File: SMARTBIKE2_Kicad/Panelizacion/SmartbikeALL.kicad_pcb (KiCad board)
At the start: 2 copper layers, 100 x 100 mm, 101 parts, among them IC1 ESP32-WROVER-B__8MB_, J1 Conn_01x02, J1 Conn_01x08, J2 Conn_01x01, J2 Conn_01x02, J2 RJ45, J3 Conn_02x03_Counter_Clockwise, J4 Conn_01x04, J5 Conn_01x05, J6 Conn_01x08, J7 Conn_01x08, J8 Conn_01x04, Q1 SI2302, Q2 FDN340P, Q3 SI2302, Q4 SI2302, Q5 SI2302, SW1 SW_Boot, SW2 SW_Reset, U1 MIC5219-3.3YM5, U1 NA555D, U2 LM358, U2 MIC29302WU, U3 MIC5219-3.3YM5, U4 NA555D

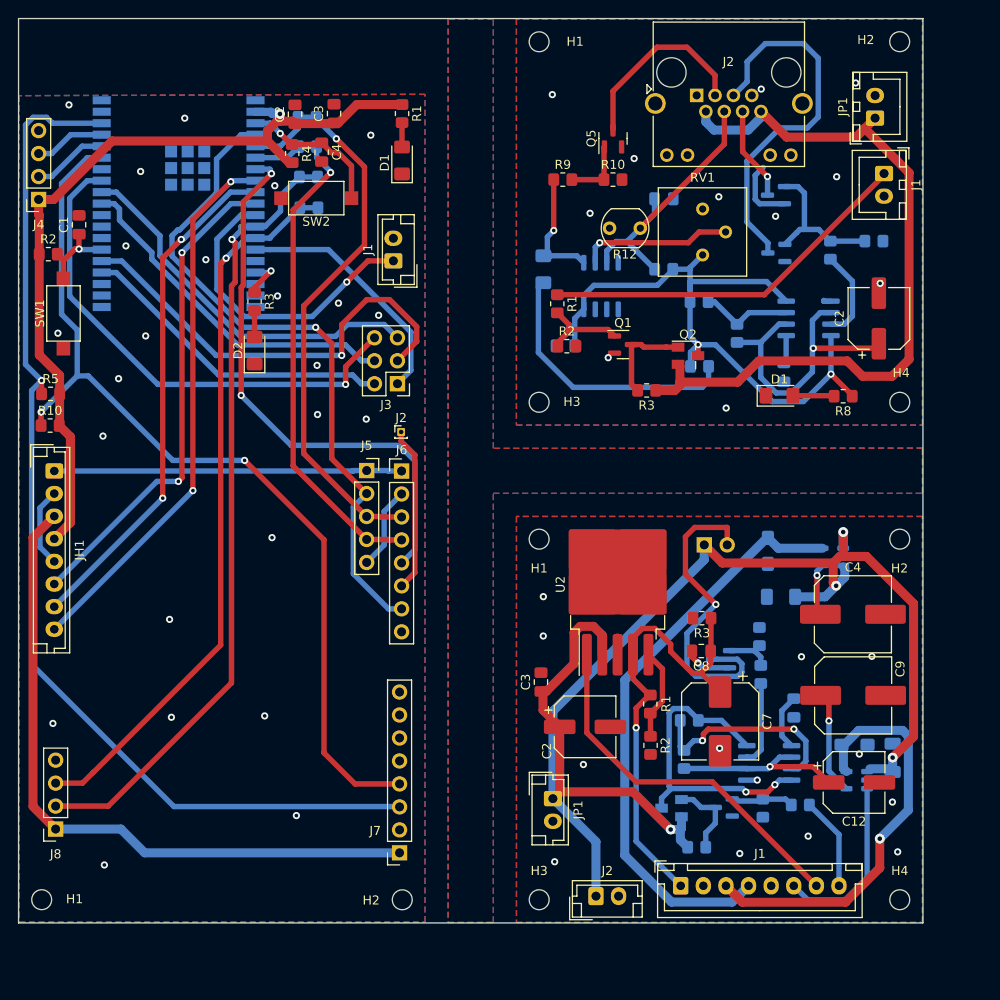
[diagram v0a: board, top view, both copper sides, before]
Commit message: Impresión vías sin metalización
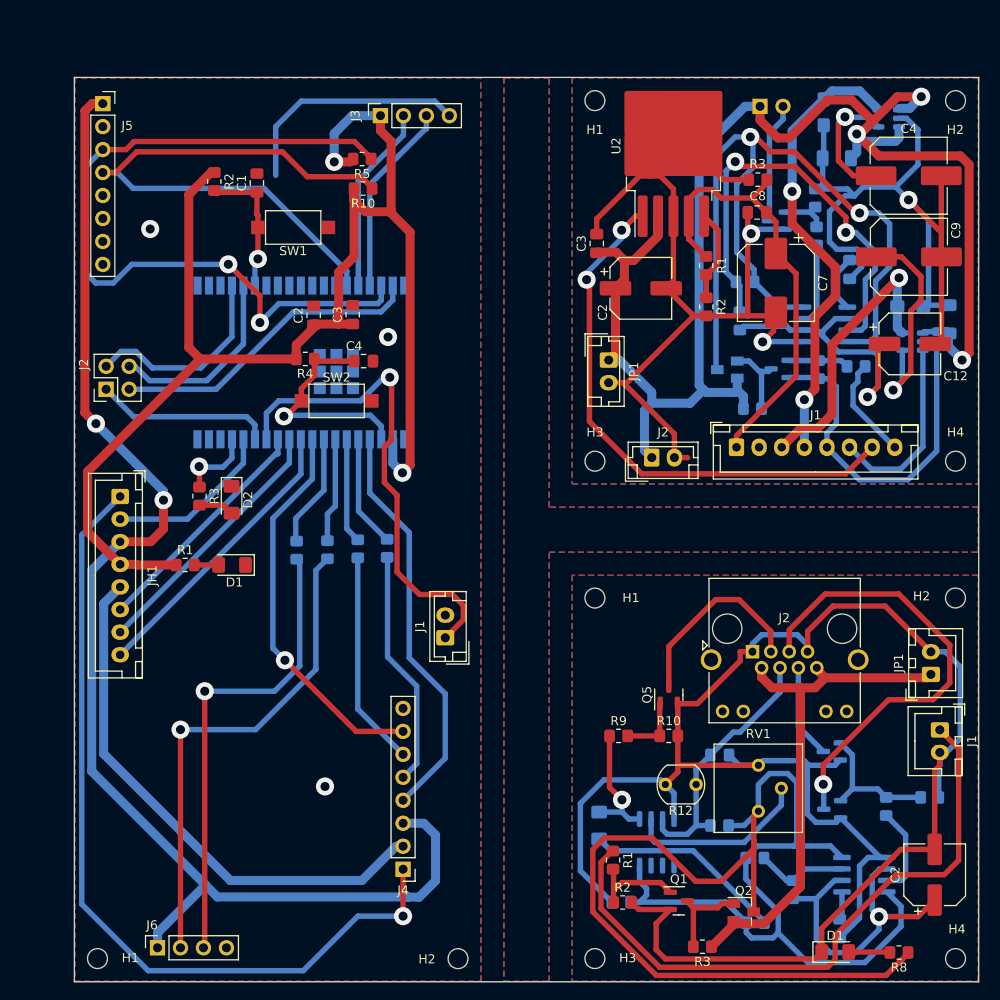
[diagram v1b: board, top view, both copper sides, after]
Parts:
- removed the C1 at (115.7, 40.8)
- removed the C1 at (193.6, 57.1)
- removed the C1 at (193.3, 81.9)
- removed the C2 at (171.6, 96.3)
- removed the C2 at (139.5, 28.5)
- removed the C2 at (204.1, 51.1)
- removed the C3 at (143.9, 28.5)
- removed the C3 at (166.7, 91.3)
- removed the C3 at (169.4, 54.1)
- removed the C4 at (201.2, 83.8)
- removed the C4 at (142.5, 32.7)
- removed the C4 at (180.3, 37.9)
- removed the D1 at (193.1, 59.7)
- removed the D1 at (151.4, 33.6)
- removed the D2 at (135.1, 54.7)
- removed the D2 at (167.0, 45.7)
- removed the H1 at (166.5, 75.5)
- removed the H1 at (166.5, 20.5)
- removed the H1 at (111.5, 115.4)
- removed the H2 at (206.4, 75.5)
- removed the H2 at (206.4, 20.5)
- removed the H2 at (151.4, 115.4)
- removed the H3 at (166.5, 60.4)
- removed the H3 at (166.5, 115.4)
- removed the H4 at (206.4, 60.4)
- removed the H4 at (206.4, 115.4)
- removed the J1 at (150.4, 44.7)
- removed the J1 at (204.7, 35.1)
- removed the J1 at (182.2, 113.8)
- removed the J2 at (151.3, 63.7)
- removed the J2 at (184.0, 26.4)
- removed the J2 at (172.8, 115.0)
- removed J7: Conn_01x08, Connector_PinSocket_2.54mm:PinSocket_1x08_P2.54mm_Vertical
- removed J8: Conn_01x04, Connector_PinSocket_2.54mm:PinSocket_1x04_P2.54mm_Vertical
- removed the JP1 at (168.1, 104.2)
- removed the JP1 at (203.7, 29.0)
- removed the Q1 at (175.8, 54.0)
- removed the Q1 at (187.0, 105.2)
- removed the Q2 at (183.0, 55.2)
- removed the Q2 at (181.2, 105.3)
- removed the Q3 at (192.7, 37.5)
- removed the Q3 at (186.7, 88.8)
- removed the R1 at (178.8, 93.8)
- removed the R1 at (151.4, 28.5)
- removed the R1 at (168.5, 49.5)
- removed the R10 at (112.5, 63.0)
- removed the R10 at (174.7, 35.8)
- removed the R10 at (190.9, 86.3)
- removed the R2 at (169.6, 54.2)
- removed the R2 at (178.8, 98.3)
- removed the R2 at (112.3, 44.0)
- removed the R3 at (184.5, 84.3)
- removed the R3 at (135.1, 49.2)
- removed the R3 at (178.4, 59.1)
- removed the R4 at (139.2, 32.9)
- removed the R4 at (198.7, 43.6)
- removed the R4 at (195.4, 104.9)
- removed the R5 at (112.5, 59.4)
- removed the R5 at (191.3, 105.3)
- removed the R5 at (203.6, 42.6)
- removed the R6 at (184.2, 49.3)
- removed the R6 at (184.0, 109.6)
- removed the R6 at (140.9, 28.9)
- removed the R7 at (140.9, 32.1)
- removed the R7 at (188.4, 52.8)
- removed the R7 at (183.1, 95.6)
- removed the R8 at (200.2, 59.7)
- removed the R8 at (141.0, 35.5)
- removed the R8 at (182.6, 99.9)
- removed the R9 at (169.2, 35.8)
- removed the R9 at (141.1, 38.9)
- removed the R9 at (191.0, 90.5)
- removed the U1 at (196.3, 51.1)
- removed the U1 at (199.0, 77.5)
- removed the U2 at (175.2, 80.6)
- removed the U2 at (173.4, 47.5)
- added C1: 0.1u, Capacitor_SMD:C_0805_2012Metric_Pad1.18x1.45mm_HandSolder, F.Cu at (135.3, 36.1)
- added C1: 10n, Capacitor_SMD:C_0805_2012Metric_Pad1.18x1.45mm_HandSolder, B.Cu at (199.8, 118.6)
- added C1: 10u, Capacitor_SMD:C_1206_3216Metric_Pad1.33x1.80mm_HandSolder, B.Cu at (199.4, 33.4)
- added C2: 22u, Capacitor_SMD:C_0805_2012Metric_Pad1.18x1.45mm_HandSolder, F.Cu at (141.6, 50.8)
- added C2: 100u, Capacitor_SMD:CP_Elec_6.3x5.4, F.Cu at (210.3, 112.6)
- added C2: 100u, Capacitor_SMD:CP_Elec_6.3x5.4, F.Cu at (177.8, 47.8)
- added C3: 1u, Capacitor_SMD:C_0805_2012Metric_Pad1.18x1.45mm_HandSolder, F.Cu at (172.9, 42.8)
- added C3: 0.1u, Capacitor_SMD:C_0805_2012Metric_Pad1.18x1.45mm_HandSolder, F.Cu at (145.9, 50.7)
- added C3: 0.1u, Capacitor_SMD:C_0805_2012Metric_Pad1.18x1.45mm_HandSolder, B.Cu at (175.6, 115.7)
- added C4: 470u, Capacitor_SMD:C_Elec_8x10.2, F.Cu at (207.4, 35.3)
- added C4: 0.1u, Capacitor_SMD:C_0805_2012Metric_Pad1.18x1.45mm_HandSolder, F.Cu at (147.1, 55.8)
- added C4: 0.1u, Capacitor_SMD:C_0805_2012Metric_Pad1.18x1.45mm_HandSolder, B.Cu at (186.5, 99.4)
- added D1: LED_ON, LED_SMD:LED_1206_3216Metric_Pad1.42x1.75mm_HandSolder, F.Cu at (132.6, 78.4)
- added D1: Power LED, LED_SMD:LED_1206_3216Metric_Pad1.42x1.75mm_HandSolder, F.Cu at (199.3, 121.2)
- added D2: LED_TEST, LED_SMD:LED_1206_3216Metric_Pad1.42x1.75mm_HandSolder, F.Cu at (132.5, 71.2)
- added D2: Detection LED, LED_SMD:LED_1206_3216Metric_Pad1.42x1.75mm_HandSolder, B.Cu at (173.2, 107.2)
- added H1: MountingHole, MountingHole:MountingHole_2.2mm_M2, F.Cu at (117.7, 121.9)
- added H1: MountingHole, MountingHole:MountingHole_2.2mm_M2, F.Cu at (172.7, 27.0)
- added H1: MountingHole, MountingHole:MountingHole_2.2mm_M2, F.Cu at (172.7, 82.0)
- added H2: MountingHole, MountingHole:MountingHole_2.2mm_M2, F.Cu at (157.6, 121.9)
- added H2: MountingHole, MountingHole:MountingHole_2.2mm_M2, F.Cu at (212.6, 82.0)
- added H2: MountingHole, MountingHole:MountingHole_2.2mm_M2, F.Cu at (212.6, 27.0)
- added H3: MountingHole, MountingHole:MountingHole_2.2mm_M2, F.Cu at (172.7, 121.9)
- added H3: MountingHole, MountingHole:MountingHole_2.2mm_M2, F.Cu at (172.7, 66.9)
- added H4: MountingHole, MountingHole:MountingHole_2.2mm_M2, F.Cu at (212.6, 121.9)
- added H4: MountingHole, MountingHole:MountingHole_2.2mm_M2, F.Cu at (212.6, 66.9)
- added J1: Conn_01x02, Connector_JST:JST_XH_B2B-XH-A_1x02_P2.50mm_Vertical, F.Cu at (210.8, 96.6)
- added J1: Conn_01x02, Connector_JST:JST_EH_B2B-EH-A_1x02_P2.50mm_Vertical, F.Cu at (156.2, 86.4)
- added J1: Conn_01x08, Connector_JST:JST_XH_B8B-XH-A_1x08_P2.50mm_Vertical, F.Cu at (188.4, 65.4)
- added J2: RJ45, Connector_RJ:RJ45_Amphenol_RJHSE538X, F.Cu at (190.1, 88.0)
- added J2: Conn_01x02, Connector_JST:JST_EH_B2B-EH-A_1x02_P2.50mm_Vertical, F.Cu at (179.0, 66.5)
- added J2: Conn_02x02_Counter_Clockwise, Connector_PinHeader_2.54mm:PinHeader_2x02_P2.54mm_Vertical, F.Cu at (118.7, 58.9)
- added JP1: Conn_01x02, Connector_JST:JST_EH_B2B-EH-A_1x02_P2.50mm_Vertical, F.Cu at (174.2, 55.7)
- added JP1: Conn_01x02, Connector_JST:JST_XH_B2B-XH-A_1x02_P2.50mm_Vertical, F.Cu at (209.8, 90.5)
- added Q1: SI2302, Package_TO_SOT_SMD:SOT-23, F.Cu at (182.0, 115.5)
- added Q1: SI2302, Package_TO_SOT_SMD:SOT-23, B.Cu at (193.1, 56.7)
- added Q2: FDN340P, Package_TO_SOT_SMD:SuperSOT-3, F.Cu at (189.2, 116.7)
- added Q2: FDN340P, Package_TO_SOT_SMD:SuperSOT-3, B.Cu at (187.3, 56.8)
- added Q3: SI2302, Package_TO_SOT_SMD:SOT-23, B.Cu at (198.9, 99.0)
- added Q3: SI2302, Package_TO_SOT_SMD:SOT-23, B.Cu at (192.8, 40.3)
- added R1: 100k, Resistor_SMD:R_0805_2012Metric_Pad1.20x1.40mm_HandSolder, F.Cu at (185.0, 45.3)
- added R1: 470, Resistor_SMD:R_0805_2012Metric_Pad1.20x1.40mm_HandSolder, F.Cu at (127.4, 78.4)
- added R1: 1k, Resistor_SMD:R_0805_2012Metric_Pad1.20x1.40mm_HandSolder, F.Cu at (174.7, 111.0)
- added R10: 100k, Resistor_SMD:R_0805_2012Metric_Pad1.20x1.40mm_HandSolder, F.Cu at (180.9, 97.3)
- added R10: 4.7k, Resistor_SMD:R_0805_2012Metric_Pad1.20x1.40mm_HandSolder, F.Cu at (147.1, 36.8)
- added R10: 100k, Resistor_SMD:R_0805_2012Metric_Pad1.20x1.40mm_HandSolder, B.Cu at (197.1, 37.8)
- added R2: 100k, Resistor_SMD:R_0805_2012Metric_Pad1.20x1.40mm_HandSolder, F.Cu at (175.8, 115.7)
- added R2: 43k, Resistor_SMD:R_0805_2012Metric_Pad1.20x1.40mm_HandSolder, F.Cu at (185.0, 49.8)
- added R2: 10k, Resistor_SMD:R_0805_2012Metric_Pad1.20x1.40mm_HandSolder, F.Cu at (130.6, 36.0)
- added R3: 470, Resistor_SMD:R_0805_2012Metric_Pad1.20x1.40mm_HandSolder, F.Cu at (129.0, 70.8)
- added R3: 470, Resistor_SMD:R_0805_2012Metric_Pad1.20x1.40mm_HandSolder, F.Cu at (190.7, 35.8)
- added R3: 100k, Resistor_SMD:R_0805_2012Metric_Pad1.20x1.40mm_HandSolder, F.Cu at (184.6, 120.6)
- added R4: 10k, Resistor_SMD:R_0805_2012Metric_Pad1.20x1.40mm_HandSolder, F.Cu at (140.7, 55.6)
- added R4: 10k, Resistor_SMD:R_0805_2012Metric_Pad1.20x1.40mm_HandSolder, B.Cu at (204.9, 105.1)
- added R4: 1k, Resistor_SMD:R_0805_2012Metric_Pad1.20x1.40mm_HandSolder, B.Cu at (201.6, 56.4)
- added R5: 4.7k, Resistor_SMD:R_0805_2012Metric_Pad1.20x1.40mm_HandSolder, F.Cu at (147.0, 33.5)
- added R5: 220k, Resistor_SMD:R_0805_2012Metric_Pad1.20x1.40mm_HandSolder, B.Cu at (209.7, 104.1)
- added R5: 100k, Resistor_SMD:R_0805_2012Metric_Pad1.20x1.40mm_HandSolder, B.Cu at (197.4, 56.8)
- added R6: 1k, Resistor_SMD:R_0805_2012Metric_Pad1.20x1.40mm_HandSolder, B.Cu at (190.4, 110.8)
- added R6: 100k, Resistor_SMD:R_0805_2012Metric_Pad1.20x1.40mm_HandSolder, B.Cu at (190.1, 61.1)
- added R6: 470, Resistor_SMD:R_0805_2012Metric_Pad1.20x1.40mm_HandSolder, B.Cu at (149.7, 76.5)
- added R7: 1k, Resistor_SMD:R_0805_2012Metric_Pad1.20x1.40mm_HandSolder, B.Cu at (189.3, 47.1)
- added R7: 2k, Resistor_SMD:R_0805_2012Metric_Pad1.20x1.40mm_HandSolder, B.Cu at (194.6, 114.3)
- added R7: 470, Resistor_SMD:R_0805_2012Metric_Pad1.20x1.40mm_HandSolder, B.Cu at (146.5, 76.6)
- added R8: 1k, Resistor_SMD:R_0805_2012Metric_Pad1.20x1.40mm_HandSolder, F.Cu at (206.3, 121.2)
- added R8: 470, Resistor_SMD:R_0805_2012Metric_Pad1.20x1.40mm_HandSolder, B.Cu at (143.1, 76.7)
- added R8: 2k, Resistor_SMD:R_0805_2012Metric_Pad1.20x1.40mm_HandSolder, B.Cu at (188.7, 51.4)
- added R9: 1k, Resistor_SMD:R_0805_2012Metric_Pad1.20x1.40mm_HandSolder, F.Cu at (175.3, 97.3)
- added R9: 1k, Resistor_SMD:R_0805_2012Metric_Pad1.20x1.40mm_HandSolder, B.Cu at (197.2, 42.0)
- added R9: 470, Resistor_SMD:R_0805_2012Metric_Pad1.20x1.40mm_HandSolder, B.Cu at (139.7, 76.7)
- added U1: MIC5219-3.3YM5, Package_TO_SOT_SMD:SOT-23-5, B.Cu at (205.2, 29.0)
- added U1: NA555D, Package_SO:SOIC-8_3.9x4.9mm_P1.27mm, B.Cu at (202.5, 112.6)
- added U2: MIC29302WU, Package_TO_SOT_SMD:TO-263-5_TabPin3, F.Cu at (181.4, 32.2)
- added U2: LM358, Package_SO:SO-8_3.9x4.9mm_P1.27mm, B.Cu at (179.5, 109.0)
- J3: value Conn_02x03_Counter_Clockwise -> Conn_01x04; footprint Connector_PinHeader_2.54mm:PinHeader_2x03_P2.54mm_Vertical -> Connector_PinSocket_2.54mm:PinSocket_1x04_P2.54mm_Vertical
- J4: value Conn_01x04 -> Conn_01x08; footprint Connector_PinSocket_2.54mm:PinSocket_1x04_P2.54mm_Vertical -> Connector_PinHeader_2.54mm:PinHeader_1x08_P2.54mm_Vertical
- J5: value Conn_01x05 -> Conn_01x08; footprint Connector_PinSocket_2.54mm:PinSocket_1x05_P2.54mm_Vertical -> Connector_PinSocket_2.54mm:PinSocket_1x08_P2.54mm_Vertical
- J6: value Conn_01x08 -> Conn_01x04; footprint Connector_PinHeader_2.54mm:PinHeader_1x08_P2.54mm_Vertical -> Connector_PinSocket_2.54mm:PinSocket_1x04_P2.54mm_Vertical
- JH1: footprint Connector_JST:JST_EH_B8B-EH-A_1x08_P2.50mm_Vertical -> Connector_JST:JST_XH_B8B-XH-A_1x08_P2.50mm_Vertical
- moved J4 84.3 mm to (151.5, 112.0)
- moved R11 61.8 mm to (186.5, 107.2)
- moved Q5 61.8 mm to (180.9, 92.7)
- moved R12 61.8 mm to (183.9, 102.6)
- moved R13 61.8 mm to (190.4, 117.9)
- moved Q4 61.8 mm to (198.9, 105.4)
- moved RV1 61.8 mm to (190.8, 105.6)
- moved J6 59.2 mm to (124.3, 120.7), turned to 90 degrees
- moved J5 50.0 mm to (118.3, 27.4)
- moved BZ1 48.9 mm to (191.0, 27.7)
- moved C10 48.9 mm to (207.6, 49.8)
- moved C12 48.9 mm to (207.5, 53.9)
- moved C5 48.9 mm to (198.0, 28.3)
- moved C6 48.9 mm to (211.8, 51.2)
- moved C7 48.9 mm to (192.7, 47.2)
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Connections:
- IC1 pad 10: /Acondicionamiento/CtrGPSAc -> /Acondicionamiento/CtrAl
- IC1 pad 11: /Acondicionamiento/CtrLuces -> /Acondicionamiento/CtrSIM
- IC1 pad 12: /Acondicionamiento/TX_GPS -> /Acondicionamiento/CtrGPSAc
- IC1 pad 13: /Acondicionamiento/RX_GPS -> /Acondicionamiento/CtrLuces
- IC1 pad 29: /Acondicionamiento/MP4 -> unconnected-(IC1-IO5-Pad29)
- IC1 pad 30: /Acondicionamiento/MP5 -> unconnected-(IC1-IO18-Pad30)
- IC1 pad 31: /Acondicionamiento/MP6 -> unconnected-(IC1-IO19-Pad31)
- IC1 pad 37: unconnected-(IC1-IO23-Pad37) -> /Acondicionamiento/MP4
- IC1 pad 5: /Acondicionamiento/TX_SIM -> /Acondicionamiento/TX_SIM_1
- IC1 pad 6: /Acondicionamiento/RX_SIM -> /Acondicionamiento/RX_SIM_1
- IC1 pad 7: /Acondicionamiento/NE_SIM -> /Acondicionamiento/TX_GPS_1
- IC1 pad 8: /Acondicionamiento/CtrAl -> /Acondicionamiento/RX_GPS_1
- IC1 pad 9: /Acondicionamiento/CtrSIM -> /Acondicionamiento/GPIO_SIM
- J3 pad 1: /Acondicionamiento/MP1 -> +3.3V
- J3 pad 2: /Acondicionamiento/MP2 -> /Acondicionamiento/RX_BOOT
- J3 pad 3: /Acondicionamiento/MP3 -> /Acondicionamiento/TX_BOOT
- J3 pad 4: /Acondicionamiento/MP4 -> GND
- J4 pad 1: +3.3V -> 4.1V
- J4 pad 2: /Acondicionamiento/RX_BOOT -> +5V
- J4 pad 3: /Acondicionamiento/TX_BOOT -> +3.3_2
- J4 pad 4: GND -> /Acondicionamiento/RST_SIM
- J5 pad 1: 4.1V -> +3.3_2
- J5 pad 2: /Acondicionamiento/RST_SIM -> GND
- J5 pad 3: /Acondicionamiento/TX_SIM -> /Acondicionamiento/SCL
- J5 pad 4: /Acondicionamiento/RX_SIM -> /Acondicionamiento/SDA
- J5 pad 5: GND -> unconnected-(J5-Pin_5-Pad5)
- J6 pad 1: 4.1V -> +3.3_2
- J6 pad 2: GND -> /Acondicionamiento/TX_GPS
- J6 pad 3: /Acondicionamiento/TX_SIM -> /Acondicionamiento/RX_GPS
- J6 pad 4: /Acondicionamiento/RX_SIM -> GND
- JH1 pad 5: GND -> +5V
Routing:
- net GND: track 54.5 -> 482.7 mm, vias 49 -> 6
- net /+VL: track 72.5 -> 165.2 mm, vias 2 -> 0
- net /Acondicionamiento/NE_SIM: track 62.1 -> 0.00 mm, vias 2 -> 0
- net +3.3_2: track 121.7 -> 178.7 mm, vias 1 -> 3
- net /Acondicionamiento/MP6: track 56.2 -> 0.00 mm, vias 1 -> 0
- net 4.1V: track 89.4 -> 143.1 mm
- net /Alarma/VA: track 35.6 -> 88.4 mm
- net +3.3V: track 157.3 -> 206.5 mm, vias 1 -> 4
- net /Acondicionamiento/GPIO_SIM: track 0.00 -> 43.1 mm, vias 0 -> 1
- net /Acondicionamiento/MP5: track 41.8 -> 0.00 mm
- net +5V: track 242.1 -> 283.7 mm, vias 4 -> 3
- net /Acondicionamiento/TX_SIM: track 64.7 -> 26.4 mm, vias 1 -> 0
- net /Acondicionamiento/SDA: track 102.9 -> 65.6 mm, vias 2 -> 0
- net /Acondicionamiento/RX_SIM: track 60.3 -> 23.8 mm, vias 1 -> 0
- net /Acondicionamiento/TX_GPS: track 88.0 -> 54.6 mm
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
